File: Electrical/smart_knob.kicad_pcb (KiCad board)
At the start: 4 copper layers, 50 x 50 mm, 75 parts, among them J1 Conn_01x04_Male, J2 USB_C_Receptacle_USB2.0, J3 Conn_01x08_Male, J4 Conn_01x03_Male, J5 Barrel_Jack_Switch, SW1 SW_SPDT, U1 DRV8311H, U2 LD3985M33R_SOT23, U3 TXU0101, U4 TLV493D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

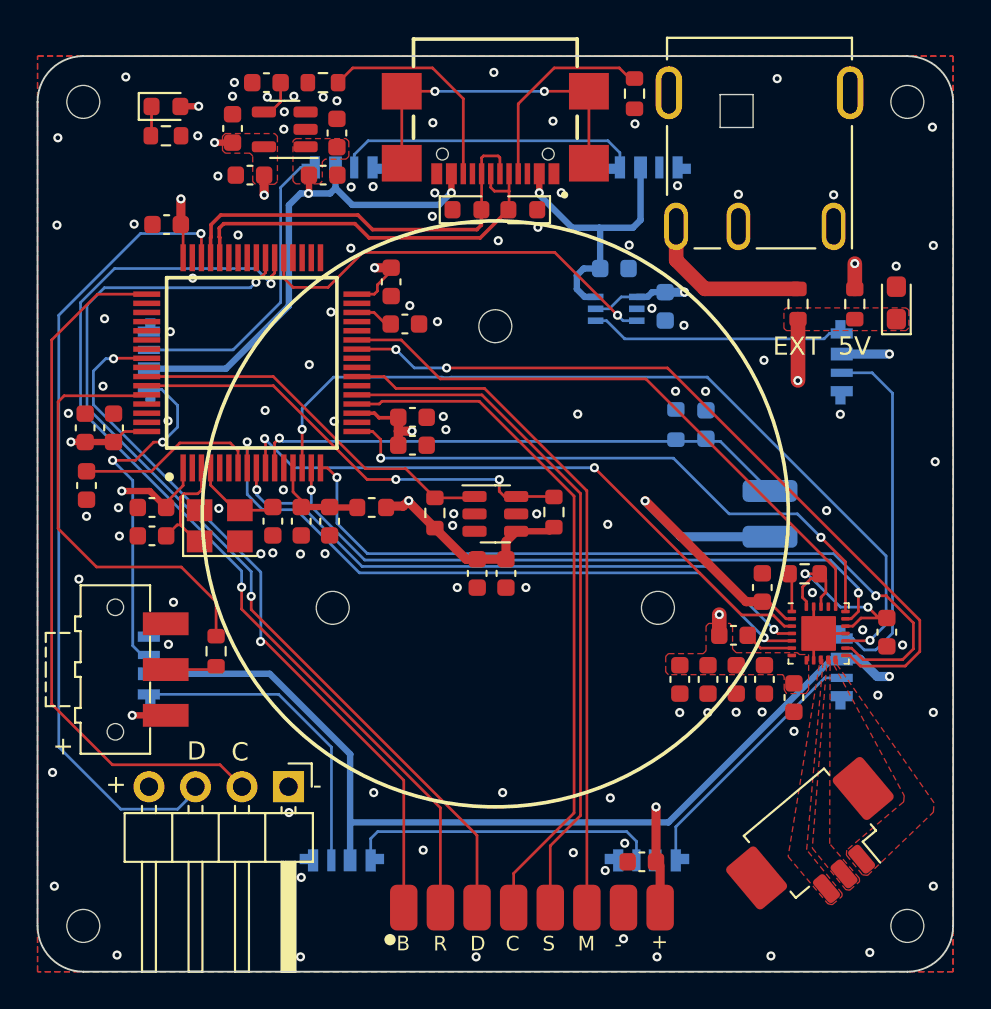
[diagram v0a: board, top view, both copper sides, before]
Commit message: fix schematic rework issues
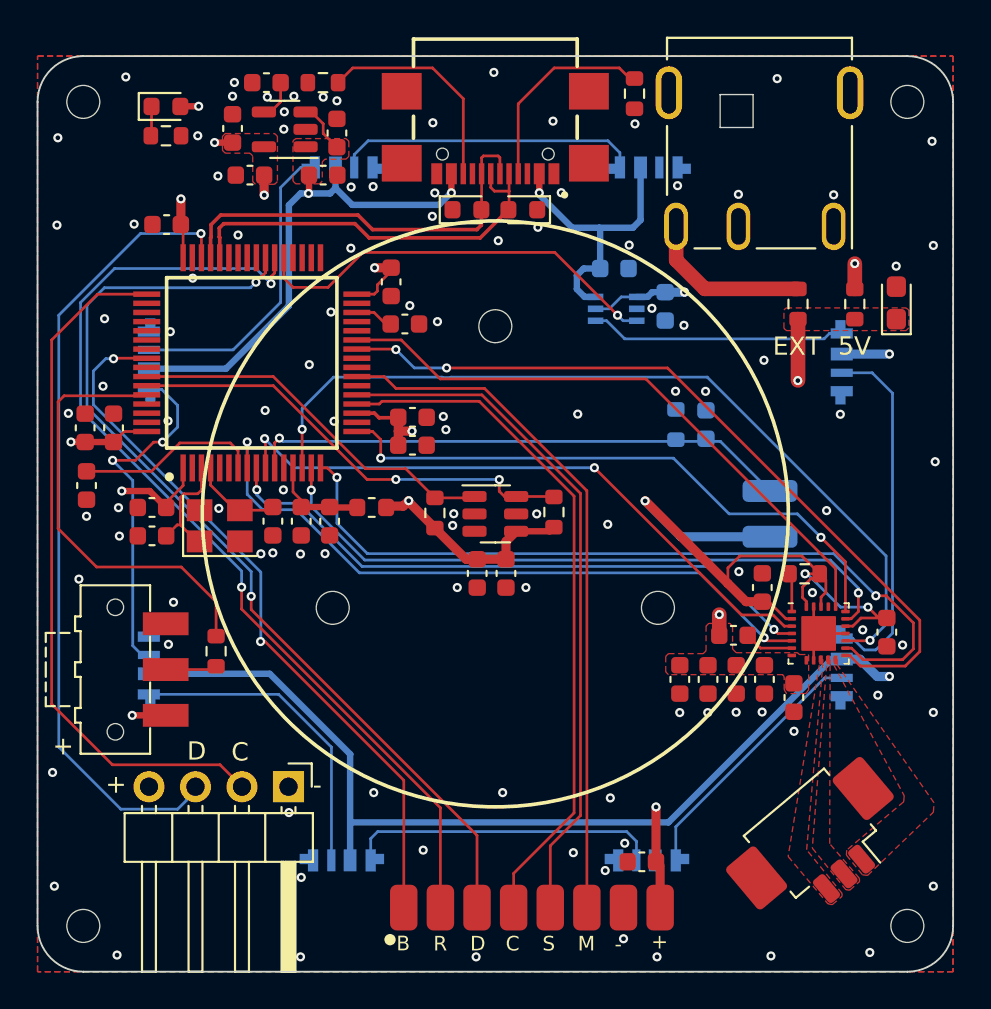
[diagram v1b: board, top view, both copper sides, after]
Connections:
- C1 pad 1: +3.3V -> AVDD
- C12 pad 2: +3.3V -> AVDD
- C15 pad 1: +3.3V -> AVDD
- C17 pad 1: +3.3V -> AVDD
- C18 pad 1: +3.3V -> AVDD
- C20 pad 1: +3.3V -> AVDD
- C21 pad 1: +3.3V -> AVDD
- C23 pad 1: +3.3V -> AVDD
- C24 pad 1: +3.3V -> AVDD
- C25 pad 1: +3.3V -> AVDD
- C26 pad 1: +3.3V -> AVDD
- C27 pad 1: +3.3V -> AVDD
- C32 pad 1: +3.3V -> AVDD
- C5 pad 1: +3.3V -> AVDD
- D3 pad 2: +3.3V -> AVDD
- FB1 pad 2: +3.3V -> AVDD
- J1 pad 4: +3.3V -> AVDD
- J3 pad 8: +3.3V -> AVDD
- R3 pad 1: +3.3V -> AVDD
- R6 pad 1: +3.3V -> AVDD
- R7 pad 1: +3.3V -> AVDD
- SW1 pad 3: +3.3V -> AVDD
- U1 pad 2: +3.3V -> AVDD
- U2 pad 3: GND -> +5V
- U2 pad 5: +3.3V -> AVDD
- U3 pad 1: +3.3V -> AVDD
- U3 pad 5: +3.3V -> AVDD
- U4 pad 4: +3.3V -> AVDD
- U5 pad 1: +3.3V -> AVDD
- U5 pad 19: +3.3V -> AVDD
- U5 pad 32: +3.3V -> AVDD
- U5 pad 48: +3.3V -> AVDD
- U5 pad 64: +3.3V -> AVDD
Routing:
- net AVDD: track 13.1 -> 203.5 mm, vias 2 -> 15
- net +3.3V: track 183.9 -> 0.00 mm, vias 13 -> 0
- net unconnected-(J2-SHIELD-PadS1): track 18.1 -> 0.00 mm, vias 2 -> 0
- net +5V: track 148.9 -> 151.7 mm
- net GND: vias 105 -> 106
- added copper zone on F.Cu, net AVDD
- removed copper zone on F.Cu, net +3.3V
